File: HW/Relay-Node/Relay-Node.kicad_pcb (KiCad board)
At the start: 2 copper layers, 70 x 50 mm, 60 parts, among them IC1 STM8S003F3P, J1 CONN_01X04, J2 CONN_01X04, J3 CONN_01X04, J4 CONN_01X04, J5 CONN_01X03, M1 NRF24L01, Q1 C1815, Q2 C1815, Q3 C1815, U1 ASM1117, U2 MC34063, U3 MAX485

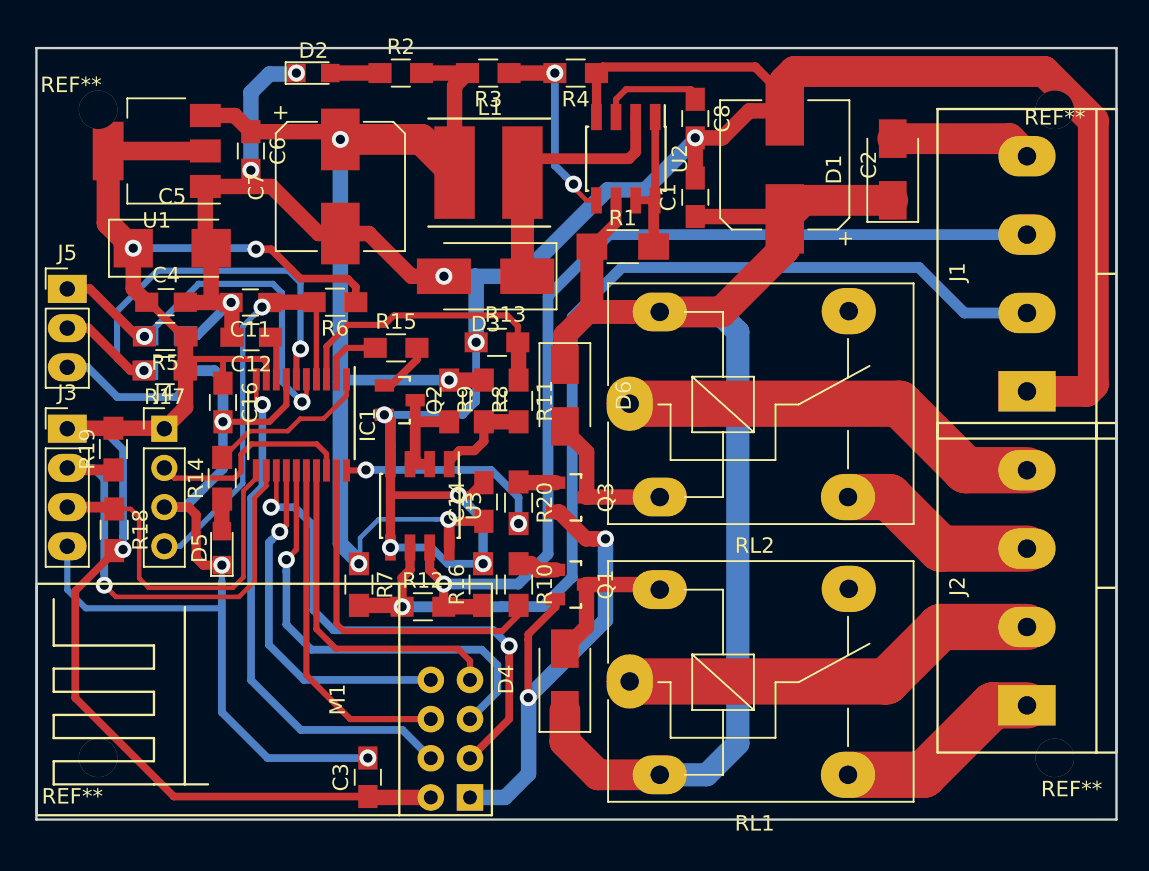
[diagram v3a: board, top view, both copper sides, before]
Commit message: complete layout pcb relay-node
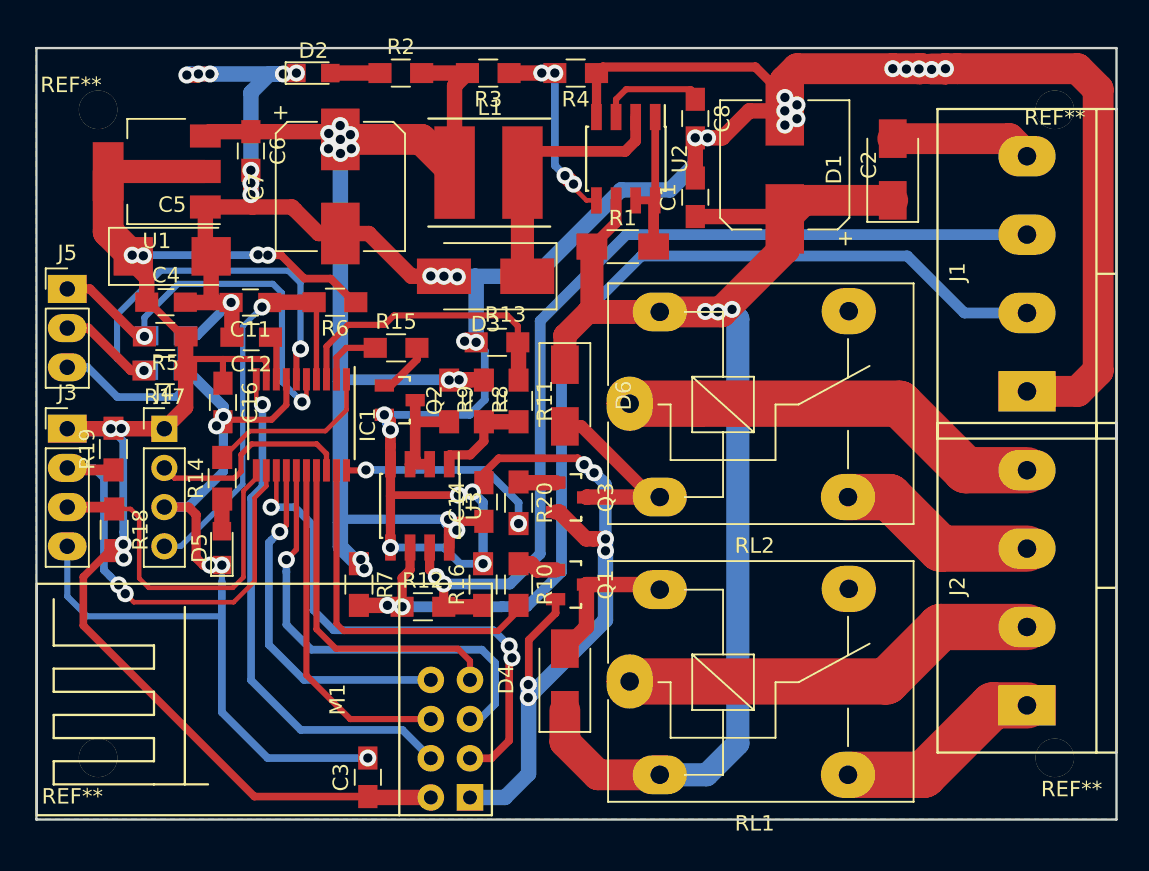
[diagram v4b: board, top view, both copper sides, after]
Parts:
- moved U1 1.33 mm to (77.8, 98.0)
- moved C5 0.53 mm to (78.8, 103.5)
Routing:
- net GND: track 284.5 -> 333.8 mm, vias 15 -> 43
- net +5V: track 76.9 -> 86.0 mm, vias 4 -> 13
- net +12V: track 91.6 -> 94.8 mm, vias 0 -> 3
- net Net-(D6-Pad2): track 9.93 -> 13.0 mm
- net +3V3: track 106.1 -> 104.2 mm, vias 3 -> 8
- net /CE: track 33.2 -> 34.9 mm, vias 2 -> 3
- net /button1: track 26.0 -> 26.8 mm
- net /SCL: track 30.6 -> 31.2 mm, vias 1 -> 2
- net Net-(IC1-Pad1): track 10.8 -> 11.3 mm
- net /A: track 67.6 -> 67.3 mm, vias 1 -> 2
- net /B: track 63.8 -> 63.5 mm, vias 1 -> 2
- net Net-(R3-Pad1): vias 2 -> 4
- added copper zone on B.Cu, net GND
- added copper zone on F.Cu, net GND

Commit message: modified label
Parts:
- added ?: , nhantt-kicad-lib:logo2, F.Cu at (85.8, 121.3)
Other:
- board text added: "nhantt"
